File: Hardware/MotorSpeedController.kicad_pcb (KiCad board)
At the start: 4 copper layers, 25.4 x 25.4 mm, 19 parts, among them J1 Conn_01x08_Female, J2 Conn_01x04_Female, U1 ATmega328P-AU, U2 AS5134, Y1 16MHz

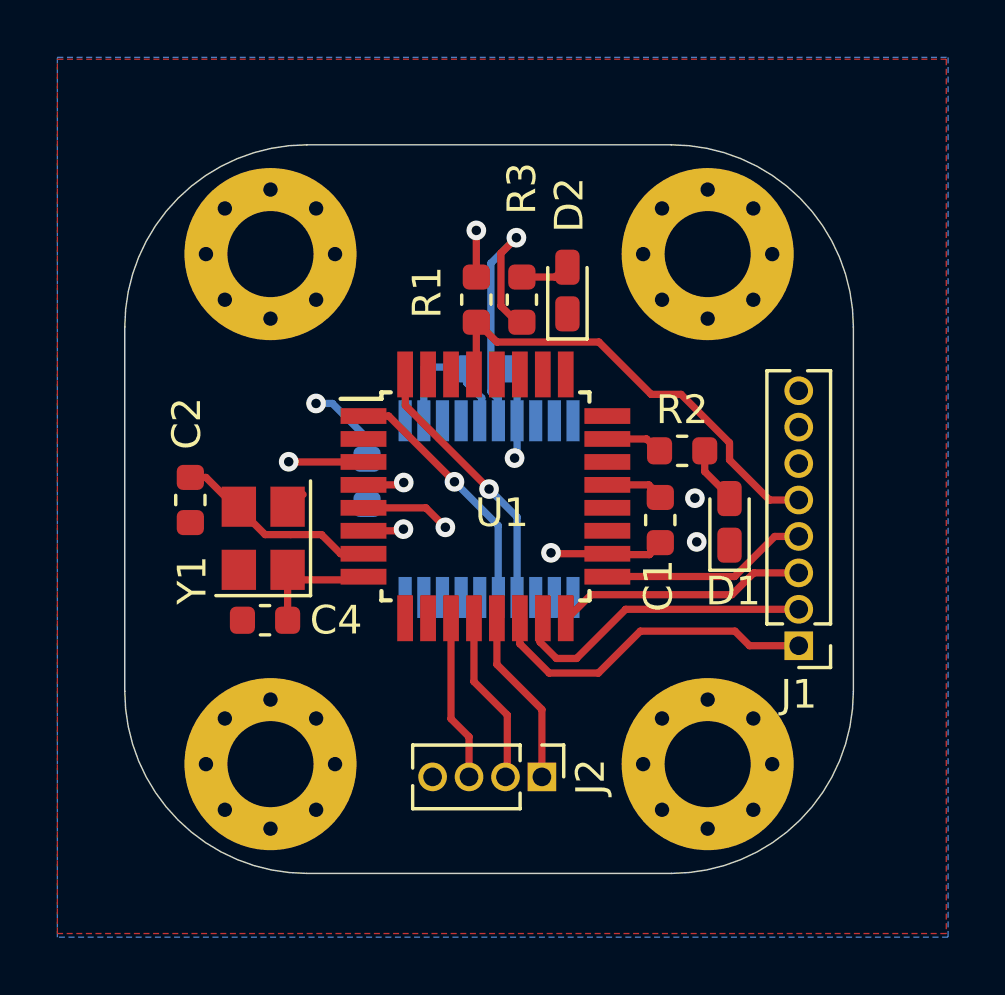
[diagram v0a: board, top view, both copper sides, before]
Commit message: Added pull downs in Interrupt pins
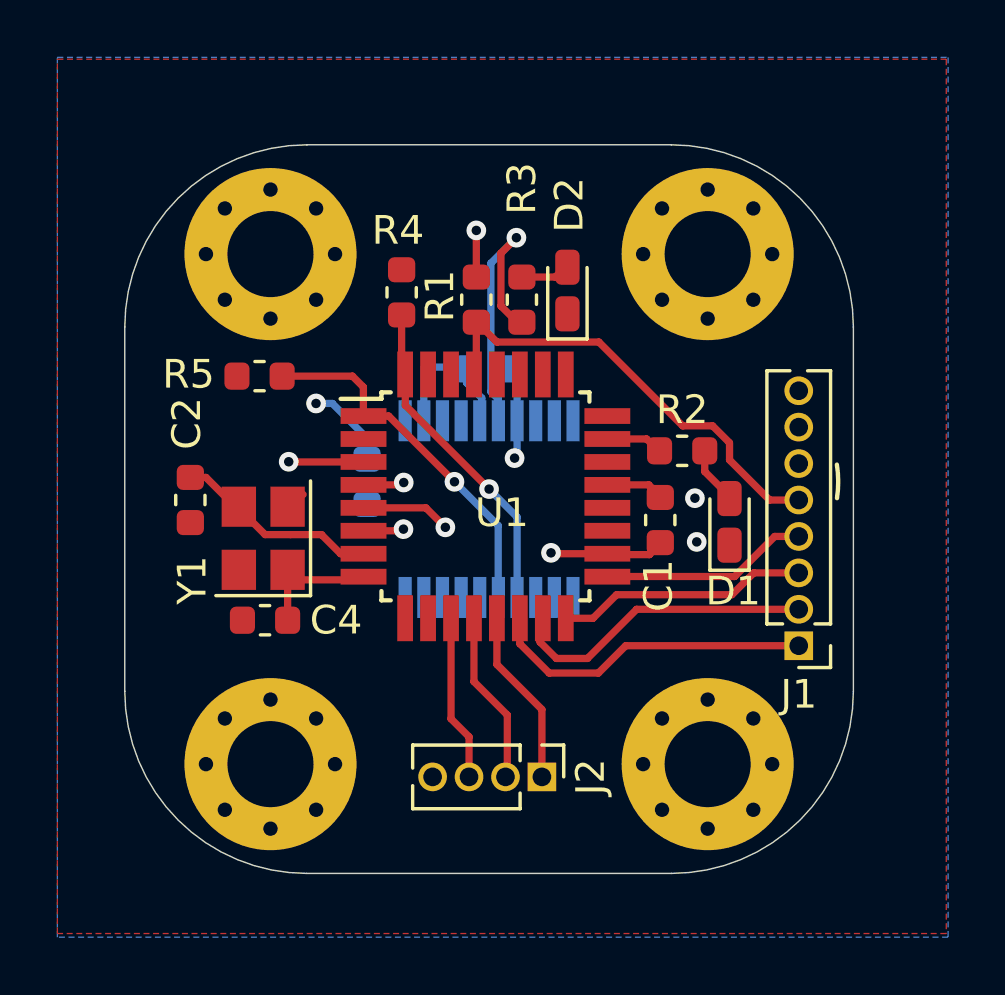
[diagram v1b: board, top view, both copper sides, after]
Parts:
- added R4: 1k, Resistor_SMD:R_0603_1608Metric, F.Cu at (111.3, 81.3)
- added R5: 1k, Resistor_SMD:R_0603_1608Metric, F.Cu at (106.3, 84.3)
- C5: value 100nF -> 0.1uF
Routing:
- net INT1: track 8.82 -> 12.8 mm
- net INT0: track 9.46 -> 11.6 mm
